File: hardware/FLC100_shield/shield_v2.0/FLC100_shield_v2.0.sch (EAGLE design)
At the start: 73 parts, among them IC1 TSR 1-2450, IC4 MCP1640SOT23-6-HAND, J1 RJ11-6PTH, Q1 2N7000, Q2 2N7000, Q3 2N7000, Q4 2N7000, Q5 2N7000, Q6 2N7000, Q7 2N7000, Q8 2N7000, Q9 2N7000, X1 RJ45, X2 CLOUD SENSOR, X4 HUMIDITY, X5 SMA

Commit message: Simplifying circuit.
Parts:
- removed JP3: MAG SDA, SparkFun:JUMPER-2PTH
- removed JP5: MAG SCL, SparkFun:JUMPER-2PTH
- removed JP7: CLOUD SDA, SparkFun:JUMPER-2PTH
- removed JP8: CLOUD SCL, SparkFun:JUMPER-2PTH
- JP1: value SHDN -> ISP VCC; device SparkFun:JUMPER-2PTH -> SparkFun:JUMPER-3PTH
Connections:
- new net N$7: JP1.2, X1.8
- net +3V3: now also JP1.3; no longer X1.8
- net 16: no longer JP7.1
- net 19: no longer JP8.1
- net CLOUD_SCL: no longer JP8.2
- net CLOUD_SDA: no longer JP7.2
- net GND: no longer JP1.1
- net MAG_SCL: no longer JP5.2
- net MAG_SDA: no longer JP3.2
- net SCL: no longer JP5.1
- net SDA: no longer JP3.1
- net SHDN: no longer JP1.2
- net VIN: now also JP1.1
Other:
- note added: "Add HIH6136 I2C version (see blog) humidity sensor. Have pull-up resistors at both ends of bus, but pull-up voltage selected on remote PCB. OR - fit HIH6136 sensor on same external PCB as used for the cloud detector?"
- note added: "Link if level shifting not required."
- note removed: "Add HIH6136 I2C version (see blog) humidity sensor. Have pull-up resistors at both ends of bus, but oull-up voltage selected on remote PCB. OR - fit HIH6136 sensor on same external PCB as used for the cloud detector?"
- note removed: "Add optional link for SHDNto GND."
- note removed: "Only fit jumper if FET omitted"
- moved on the sheet: J1

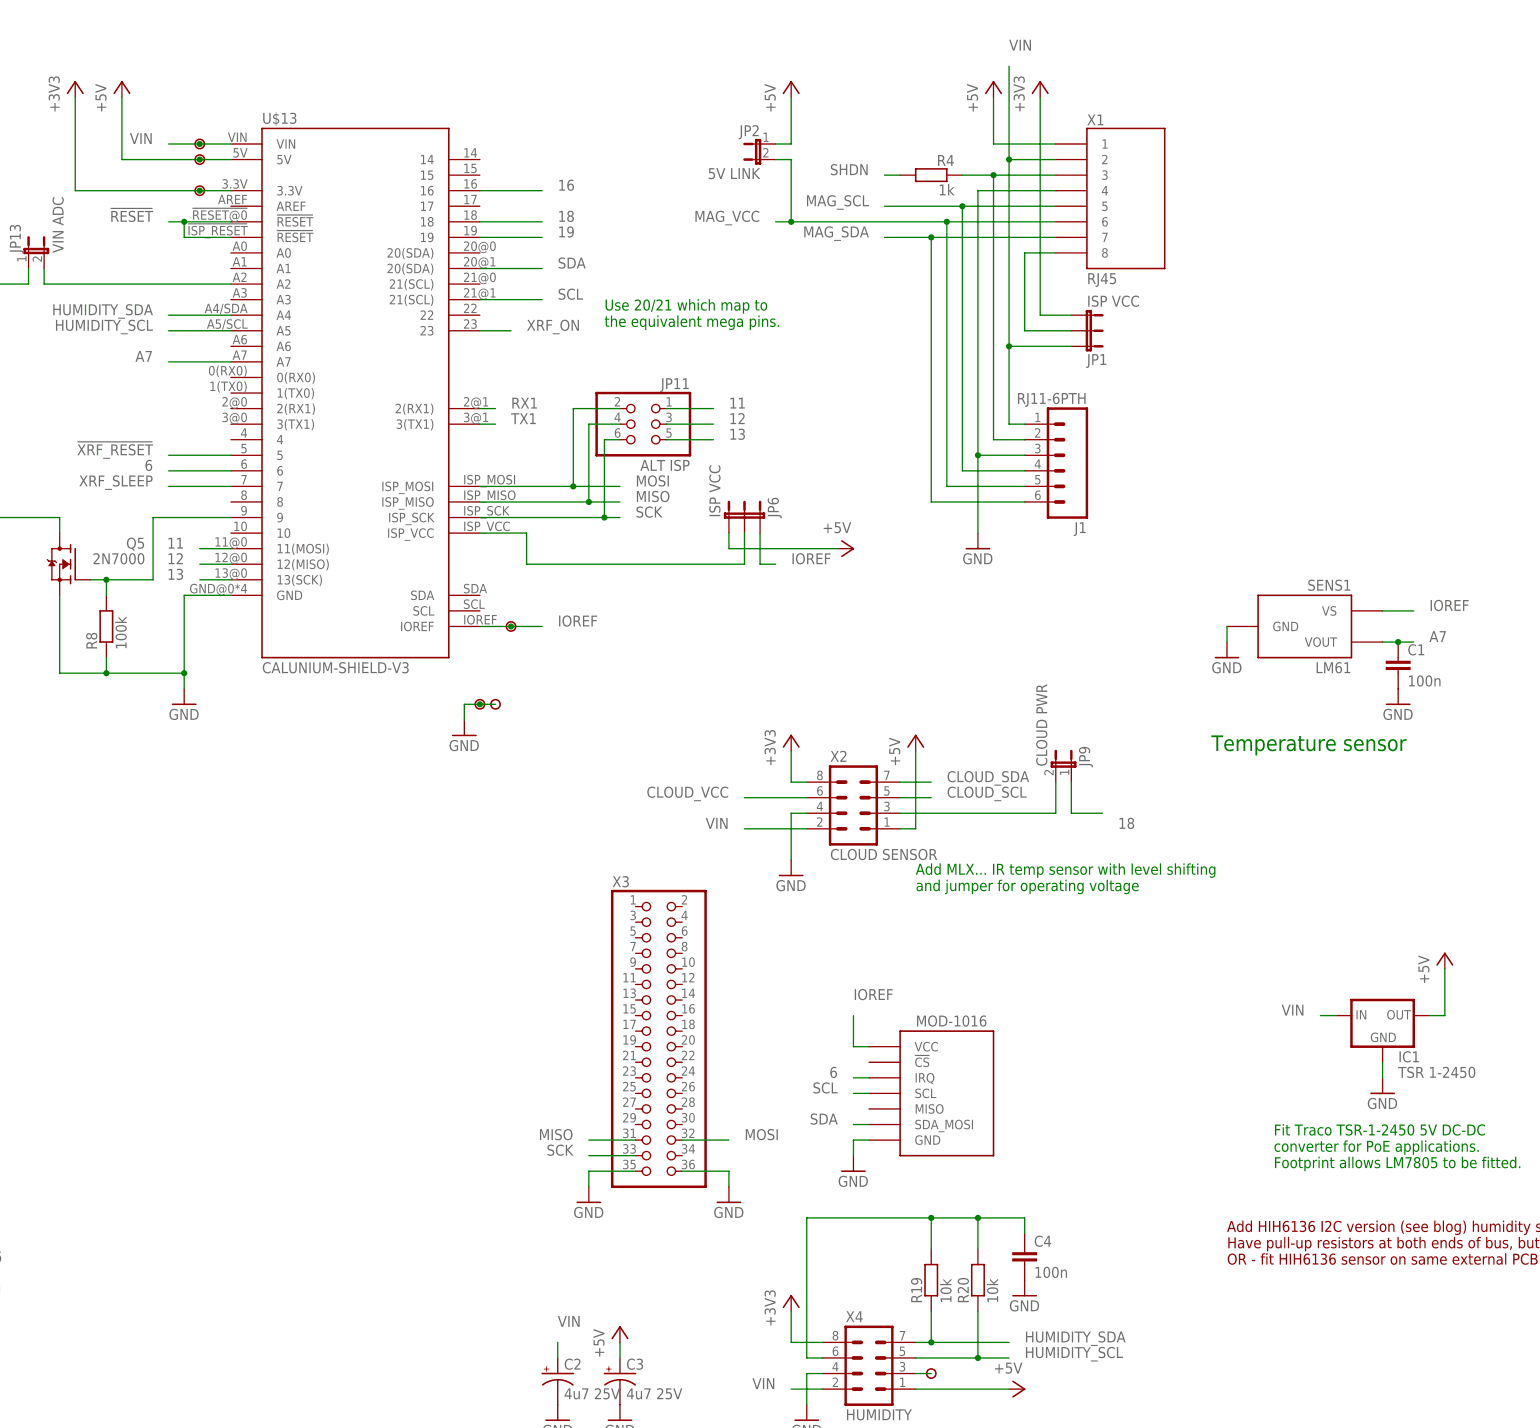
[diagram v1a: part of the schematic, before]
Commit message: Tidying silkscreen.
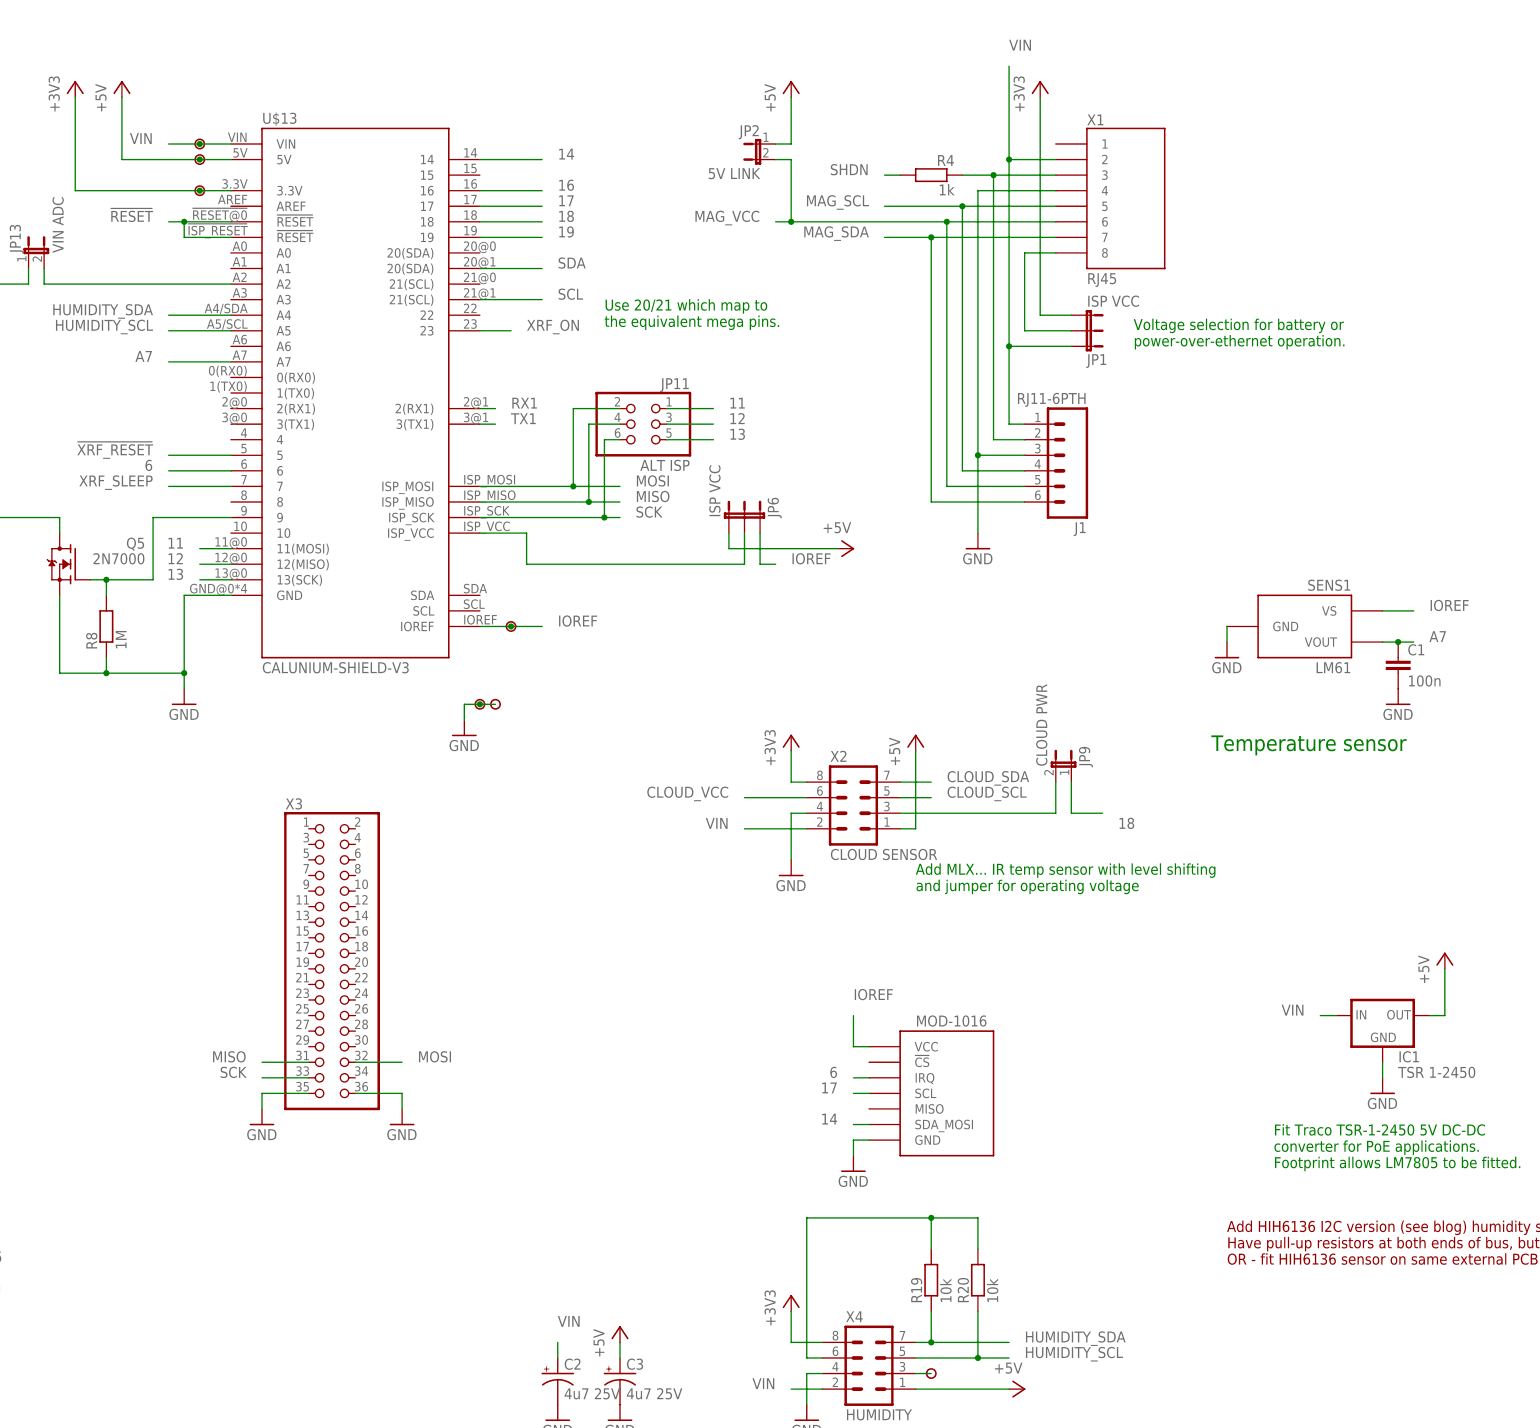
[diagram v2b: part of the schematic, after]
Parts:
- removed C4: 100n, SparkFun:CAPPTH
- R8: value 100k -> 1M
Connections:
- new net 14: MOD-1016.SDA_MOSI, U$13.14
- new net 17: MOD-1016.SCL, U$13.17
- net +5V: no longer X1.1
- net GND: no longer C4.2
- net N$22: no longer C4.1
- net SCL: no longer MOD-1016.SCL
- net SDA: no longer MOD-1016.SDA_MOSI
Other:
- note added: "Voltage selection for battery or power-over-ethernet operation."
- moved on the sheet: X3
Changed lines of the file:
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@@
 <setting verticaltext="up"/>
 </settings>
-<grid distance="0.1" unitdist="inch" unit="inch" style="lines" multiple="1" display="yes" altdistance="0.01" altunitdist="inch" altunit="inch"/>
+<grid distance="0.1" unitdist="inch" unit="inch" style="lines" multiple="1" display="no" altdistance="0.01" altunitdist="inch" altunit="inch"/>
 <layers>
 <layer number="1" name="Top" color="4" fill="1" visible="no" active="no"/>
@@
 <part name="C1" library="SparkFun" deviceset="CAP" device="PTH" value="100n"/>
 <part name="GND23" library="supply1" deviceset="GND" device=""/>
-<part name="R8" library="SteveMarple" deviceset="RESISTOR" device="" value="100k"/>
+<part name="R8" library="SteveMarple" deviceset="RESISTOR" device="" value="1M"/>
 <part name="U$14" library="SteveMarple" deviceset="PAD" device=""/>
 <part name="U$1" library="SteveMarple" deviceset="PAD" device=""/>
@@
 <part name="R20" library="SteveMarple" deviceset="RESISTOR" device="" value="10k"/>
 <part name="P+6" library="supply1" deviceset="+5V" device=""/>
-<part name="P+10" library="supply1" deviceset="+5V" device=""/>
 <part name="P+11" library="supply1" deviceset="+5V" device=""/>
 <part name="C3" library="SparkFun" deviceset="CAP_POL" device="PTH2" value="4u7 25V"/>
@@
 <part name="X5" library="SteveMarple" deviceset="CONN-SMA" device="THD-SMD-EDGE" value="SMA"/>
 <part name="GND14" library="supply1" deviceset="GND" device=""/>
-<part name="C4" library="SparkFun" deviceset="CAP" device="PTH" value="100n"/>
-<part name="GND21" library="supply1" deviceset="GND" device=""/>
 <part name="JP1" library="SparkFun" deviceset="JUMPER-3" device="PTH" value="ISP VCC"/>
 </parts>
@@
 <wire x1="50.8" y1="86.36" x2="91.44" y2="86.36" width="0.1524" layer="94" style="shortdash"/>
 <wire x1="91.44" y1="86.36" x2="96.52" y2="91.44" width="0.1524" layer="94" style="shortdash"/>
+<text x="317.5" y="200.66" size="1.778" layer="91">Voltage selection for battery or
+power-over-ethernet operation.</text>
 </plain>
 <instances>
@@
 <instance part="P+1" gate="1" x="261.62" y="243.84"/>
 <instance part="+3V1" gate="G$1" x="302.26" y="243.84"/>
-<instance part="X3" gate="A" x="238.76" y="88.9"/>
-<instance part="GND1" gate="1" x="228.6" y="60.96"/>
-<instance part="GND2" gate="1" x="251.46" y="60.96"/>
+<instance part="X3" gate="A" x="185.42" y="101.6"/>
+<instance part="GND1" gate="1" x="175.26" y="73.66"/>
+<instance part="GND2" gate="1" x="198.12" y="73.66"/>
 <instance part="P+3" gate="1" x="71.12" y="243.84"/>
 <instance part="P+4" gate="1" x="71.12" y="205.74"/>
@@
 <instance part="R20" gate="G$1" x="292.1" y="48.26" rot="R90"/>
 <instance part="P+6" gate="1" x="281.94" y="137.16"/>
-<instance part="P+10" gate="1" x="294.64" y="243.84"/>
 <instance part="P+11" gate="1" x="299.72" y="30.48" rot="R270"/>
 <instance part="C3" gate="G$1" x="233.68" y="33.02"/>
@@
 <instance part="X5" gate="G$1" x="205.74" y="-104.14" rot="MR0"/>
 <instance part="GND14" gate="1" x="205.74" y="-111.76"/>
-<instance part="C4" gate="G$1" x="299.72" y="50.8"/>
-<instance part="GND21" gate="1" x="299.72" y="45.72"/>
 <instance part="JP1" gate="G$1" x="309.88" y="200.66" rot="MR90"/>
 </instances>
@@
 </segment>
 <segment>
-<pinref part="X1" gate="G$1" pin="1"/>
-<wire x1="304.8" y1="233.68" x2="294.64" y2="233.68" width="0.1524" layer="91"/>
-<pinref part="P+10" gate="1" pin="+5V"/>
-<wire x1="294.64" y1="241.3" x2="294.64" y2="233.68" width="0.1524" layer="91"/>
-</segment>
-<segment>
 <pinref part="X4" gate="G$1" pin="1"/>
 <wire x1="297.18" y1="30.48" x2="281.94" y2="30.48" width="0.1524" layer="91"/>
@@
 </net>
 <net name="SCL" class="0">
-<segment>
-<pinref part="MOD-1016" gate="G$1" pin="SCL"/>
-<wire x1="274.32" y1="78.74" x2="271.78" y2="78.74" width="0.1524" layer="91"/>
-<label x="269.24" y="78.74" size="1.778" layer="95" rot="MR0"/>
-</segment>
 <segment>
 <pinref part="R5" gate="G$1" pin="1"/>
@@
 <pinref part="X3" gate="A" pin="36"/>
 <pinref part="GND2" gate="1" pin="GND"/>
-<wire x1="243.84" y1="66.04" x2="251.46" y2="66.04" width="0.1524" layer="91"/>
-<wire x1="251.46" y1="66.04" x2="251.46" y2="63.5" width="0.1524" layer="91"/>
+<wire x1="190.5" y1="78.74" x2="198.12" y2="78.74" width="0.1524" layer="91"/>
+<wire x1="198.12" y1="78.74" x2="198.12" y2="76.2" width="0.1524" layer="91"/>
 </segment>
 <segment>
 <pinref part="X3" gate="A" pin="35"/>
 <pinref part="GND1" gate="1" pin="GND"/>
-<wire x1="236.22" y1="66.04" x2="228.6" y2="66.04" width="0.1524" layer="91"/>
-<wire x1="228.6" y1="66.04" x2="228.6" y2="63.5" width="0.1524" layer="91"/>
+<wire x1="182.88" y1="78.74" x2="175.26" y2="78.74" width="0.1524" layer="91"/>
+<wire x1="175.26" y1="78.74" x2="175.26" y2="76.2" width="0.1524" layer="91"/>
 </segment>
 <segment>
@@
 <pinref part="X5" gate="G$1" pin="GND"/>
 <pinref part="GND14" gate="1" pin="GND"/>
-</segment>
-<segment>
-<pinref part="C4" gate="G$1" pin="2"/>
-<pinref part="GND21" gate="1" pin="GND"/>
 </segment>
 </net>
@@
 <net name="SDA" class="0">
 <segment>
-<pinref part="MOD-1016" gate="G$1" pin="SDA_MOSI"/>
-<wire x1="274.32" y1="73.66" x2="271.78" y2="73.66" width="0.1524" layer="91"/>
-<label x="269.24" y="73.66" size="1.778" layer="95" rot="MR0"/>
-</segment>
-<segment>
 <pinref part="R1" gate="G$1" pin="1"/>
 <wire x1="45.72" y1="226.06" x2="45.72" y2="228.6" width="0.1524" layer="91"/>
@@
 <segment>
 <pinref part="X3" gate="A" pin="32"/>
-<wire x1="243.84" y1="71.12" x2="251.46" y2="71.12" width="0.1524" layer="91"/>
-<label x="254" y="71.12" size="1.778" layer="95"/>
+<wire x1="190.5" y1="83.82" x2="198.12" y2="83.82" width="0.1524" layer="91"/>
+<label x="200.66" y="83.82" size="1.778" layer="95"/>
 </segment>
 </net>
@@
 <segment>
 <pinref part="X3" gate="A" pin="31"/>
-<wire x1="236.22" y1="71.12" x2="228.6" y2="71.12" width="0.1524" layer="91"/>
-<label x="226.06" y="71.12" size="1.778" layer="95" rot="MR0"/>
+<wire x1="182.88" y1="83.82" x2="175.26" y2="83.82" width="0.1524" layer="91"/>
+<label x="172.72" y="83.82" size="1.778" layer="95" rot="MR0"/>
 </segment>
 </net>
@@
 <segment>
 <pinref part="X3" gate="A" pin="33"/>
-<wire x1="236.22" y1="68.58" x2="228.6" y2="68.58" width="0.1524" layer="91"/>
-<label x="226.06" y="68.58" size="1.778" layer="95" rot="MR0"/>
+<wire x1="182.88" y1="81.28" x2="175.26" y2="81.28" width="0.1524" layer="91"/>
+<label x="172.72" y="81.28" size="1.778" layer="95" rot="MR0"/>
 </segment>
 </net>
@@
 <pinref part="R19" gate="G$1" pin="2"/>
 <wire x1="284.48" y1="53.34" x2="284.48" y2="58.42" width="0.1524" layer="91"/>
-<junction x="292.1" y="58.42"/>
-<pinref part="C4" gate="G$1" pin="1"/>
-<wire x1="292.1" y1="58.42" x2="299.72" y2="58.42" width="0.1524" layer="91"/>
-<wire x1="299.72" y1="58.42" x2="299.72" y2="55.88" width="0.1524" layer="91"/>
 </segment>
 </net>
@@
 </segment>
 </net>
+<net name="14" class="0">
+<segment>
+<pinref part="U$13" gate="G$1" pin="14"/>
+<wire x1="210.82" y1="231.14" x2="220.98" y2="231.14" width="0.1524" layer="91"/>
+<label x="223.52" y="231.14" size="1.778" layer="95"/>
+</segment>
+<segment>
+<pinref part="MOD-1016" gate="G$1" pin="SDA_MOSI"/>
+<wire x1="274.32" y1="73.66" x2="271.78" y2="73.66" width="0.1524" layer="91"/>
+<label x="269.24" y="73.66" size="1.778" layer="95" rot="MR0"/>
+</segment>
+</net>
+<net name="17" class="0">
+<segment>
+<pinref part="U$13" gate="G$1" pin="17"/>
+<wire x1="210.82" y1="223.52" x2="220.98" y2="223.52" width="0.1524" layer="91"/>
+<label x="223.52" y="223.52" size="1.778" layer="95"/>
+</segment>
+<segment>
+<pinref part="MOD-1016" gate="G$1" pin="SCL"/>
+<wire x1="274.32" y1="78.74" x2="271.78" y2="78.74" width="0.1524" layer="91"/>
+<label x="269.24" y="78.74" size="1.778" layer="95" rot="MR0"/>
+</segment>
+</net>
